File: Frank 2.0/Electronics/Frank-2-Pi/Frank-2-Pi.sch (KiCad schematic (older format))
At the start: 62 parts, among them J1 left wheel sensor, J10 USB-to-controller, J11 power-connector, J12 servo 3, J13 servo 2, J14 servo 1, J15 GPIO, J16 data-connector, J2 Left motor, J3 Right motor, J4 right wheel sensor, J5 Analogue inputs, J6 LIDAR, J7 Phototransistor, J8 USB-from-battery, J9 power switch, Q1 DMN6075S, Q2 DMN6075S, U1 adafruit-2448, U2 LM2903, U3 adafruit-1015, U4 AP1117-33, U5 sparkfun-sx1509

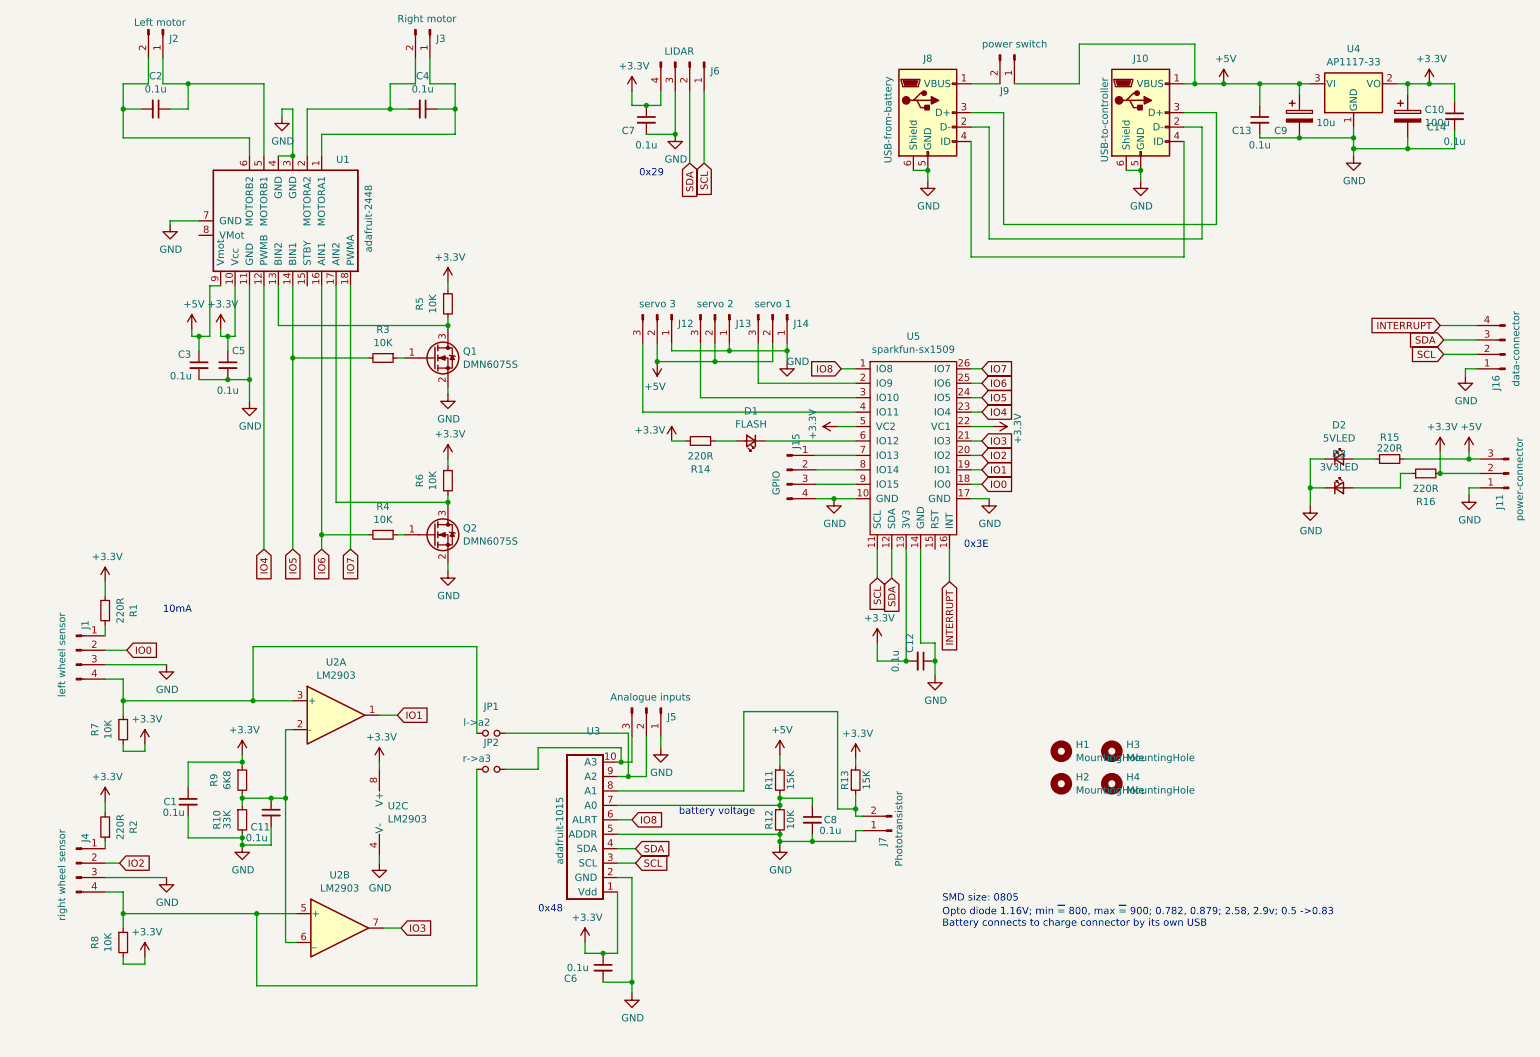
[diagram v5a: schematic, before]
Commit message: PCB finished (but probably not final...) Except for silks
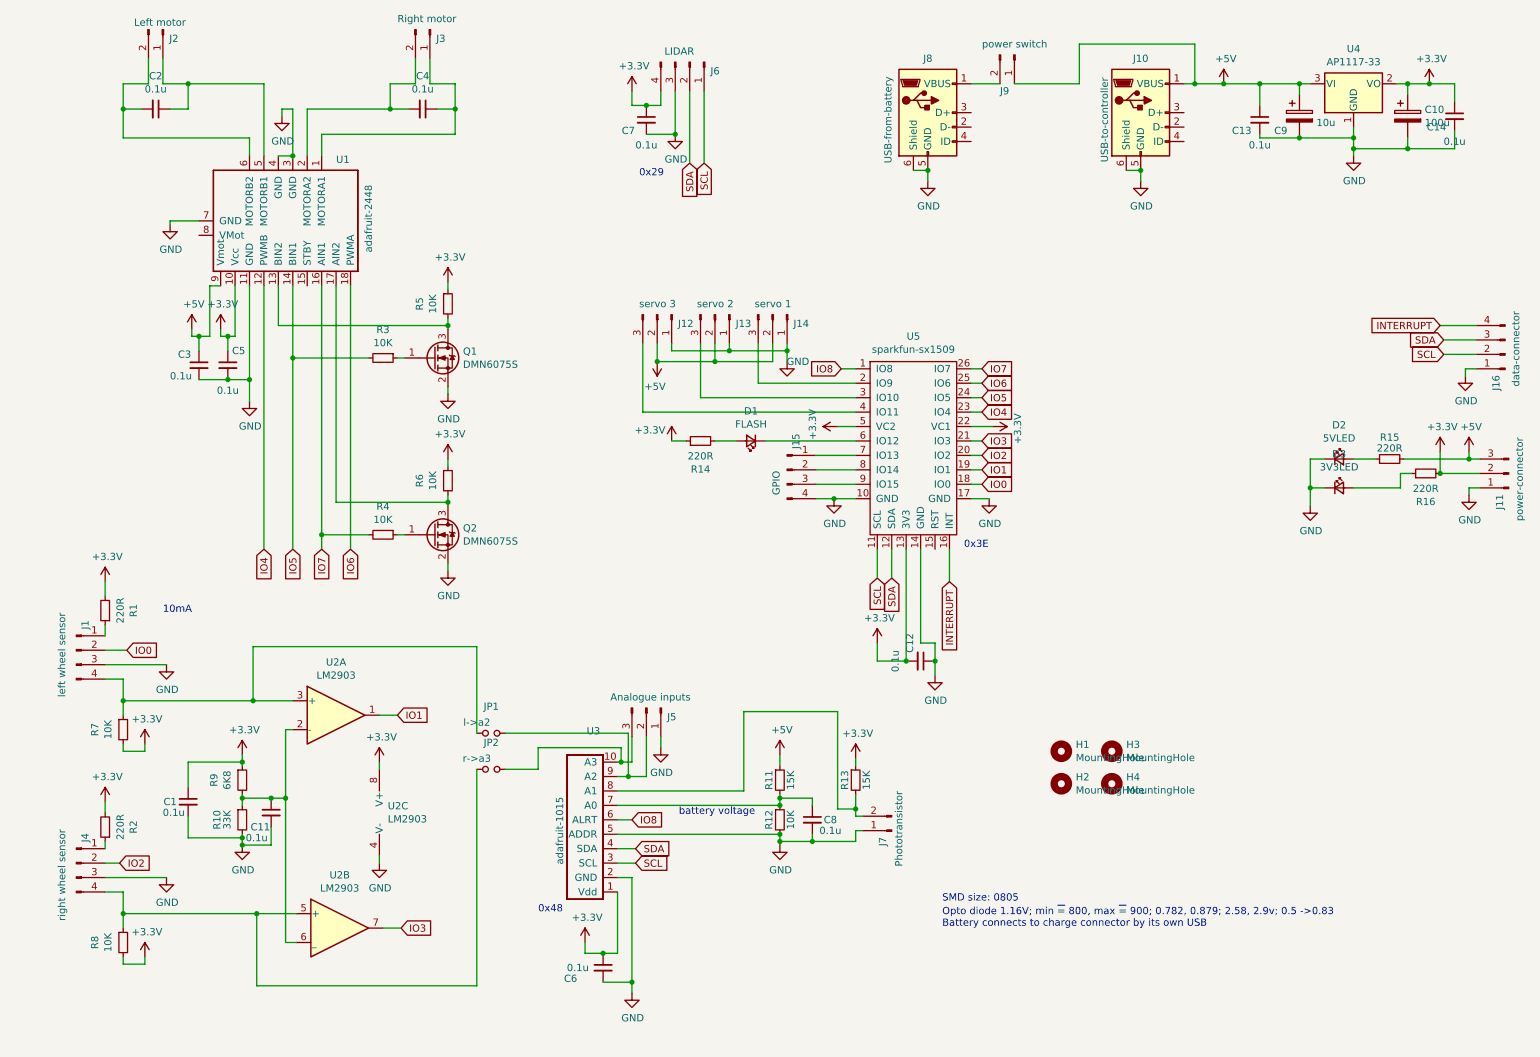
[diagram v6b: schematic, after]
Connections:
- net IO6: now also U1.18 (PWMA); no longer R4.2, U1.16 (AIN1)
- net IO7: now also R4.2, U1.16 (AIN1); no longer U1.18 (PWMA)
- net at J10.2 (D-): no longer J8.2 (D-)
- net at J10.3 (D+): no longer J8.3 (D+)
- net at J10.4 (ID): no longer J8.4 (ID)
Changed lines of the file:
@@
 IO4
 Text GLabel 2925 4225 3    50   Input ~ 0
-IO7
+IO6
 Text GLabel 2525 4225 3    50   Input ~ 0
 IO5
 Text GLabel 2725 4225 3    50   Input ~ 0
-IO6
+IO7
 $Comp
 L Transistor_FET:DMN6075S Q1
@@
 Wire Wire Line
 	8400 1600 8400 1675
-Wire Wire Line
-	8700 1200 8925 1200
-Wire Wire Line
-	8700 1300 8825 1300
 $Comp
 L Connector:USB_OTG J8
@@
 Wire Wire Line
 	6925 1600 6925 1675
-Wire Wire Line
-	7225 1200 7450 1200
-Wire Wire Line
-	7225 1300 7350 1300
-Wire Wire Line
-	8925 1200 8925 1975
-Wire Wire Line
-	7450 1200 7450 1975
-Wire Wire Line
-	8825 1300 8825 2075
-Wire Wire Line
-	7350 1300 7350 2075
-Wire Wire Line
-	7450 1975 8925 1975
-Wire Wire Line
-	7350 2075 8825 2075
 $Comp
 L Connector:Conn_01x02_Male J9
@@
 Wire Wire Line
 	10650 2975 10650 3025
-Wire Wire Line
-	7225 1400 7225 2200
-Wire Wire Line
-	7225 2200 8700 2200
-Wire Wire Line
-	8700 2200 8700 1400
 Text Notes 4925 1650 0    50   ~ 0
 0x29

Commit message: Motor and castor design improvements. I2C pullup resistors added.
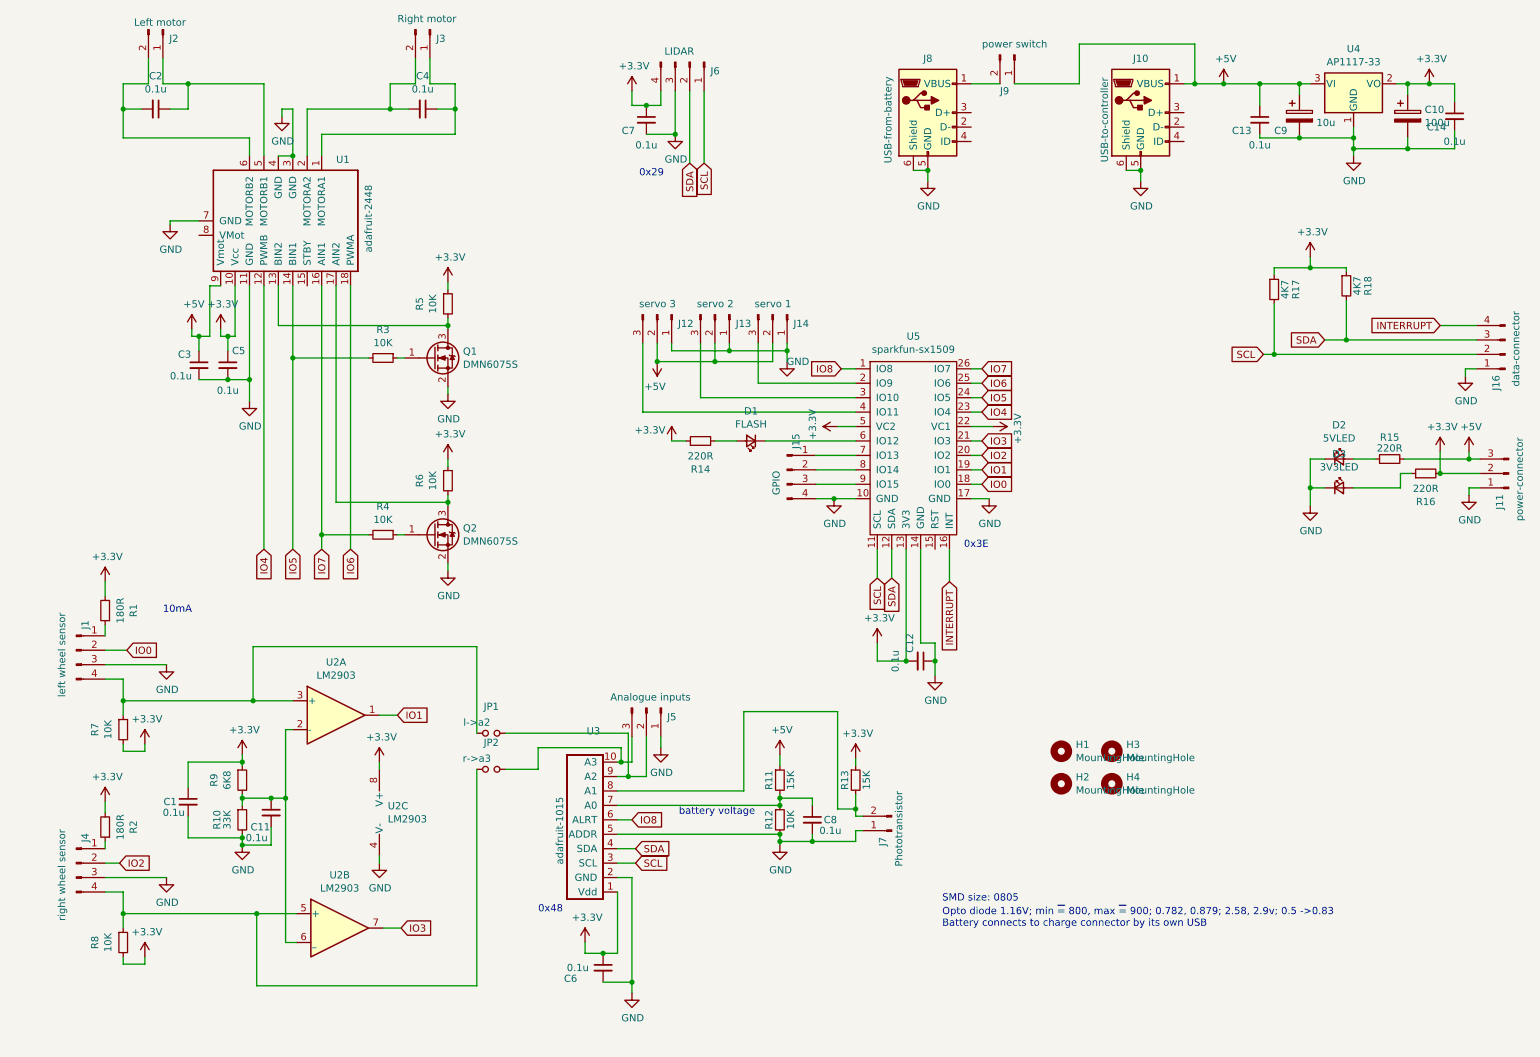
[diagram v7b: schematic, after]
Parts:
- added R17, R18: 4K7, Resistor_SMD:R_0805_2012Metric, symbol Device:R_Small
- R1, R2: value 220R -> 180R
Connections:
- net +3V3: now also R17.1, R18.1
- net SCL: now also R17.2
- net SDA: now also R18.2
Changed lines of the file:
@@
 P 1225 4650
 F 0 "R1" V 1029 4650 50  0000 C CNN
-F 1 "220R" V 1120 4650 50  0000 C CNN
+F 1 "180R" V 1120 4650 50  0000 C CNN
 F 2 "Resistor_SMD:R_0805_2012Metric" H 1225 4650 50  0001 C CNN
 F 3 "~" H 1225 4650 50  0001 C CNN
@@
 P 1225 6150
 F 0 "R2" V 1029 6150 50  0000 C CNN
-F 1 "220R" V 1120 6150 50  0000 C CNN
+F 1 "180R" V 1120 6150 50  0000 C CNN
 F 2 "Resistor_SMD:R_0805_2012Metric" H 1225 6150 50  0001 C CNN
 F 3 "~" H 1225 6150 50  0001 C CNN
@@
 	1    0    0    -1
 $EndComp
-Text GLabel 10500 2775 0    50   Input ~ 0
+Text GLabel 9675 2775 0    50   Input ~ 0
 SDA
-Text GLabel 10500 2875 0    50   Input ~ 0
+Text GLabel 9250 2875 0    50   Input ~ 0
 SCL
-Wire Wire Line
-	10500 2775 10725 2775
-Wire Wire Line
-	10500 2875 10725 2875
 Wire Wire Line
 	10725 2975 10650 2975
@@
 	1    0    0    -1
 $EndComp
+Wire Wire Line
+	9675 2775 9825 2775
+Wire Wire Line
+	10725 2875 9325 2875
+$Comp
+L Device:R_Small R18
+U 1 1 5F395C16
+P 9825 2400
+F 0 "R18" V 9975 2400 50  0000 C CNN
+F 1 "4K7" V 9900 2400 50  0000 C CNN
+F 2 "Resistor_SMD:R_0805_2012Metric" H 9825 2400 50  0001 C CNN
+F 3 "~" H 9825 2400 50  0001 C CNN
+	1    9825 2400
+	1    0    0    -1
+$EndComp
+$Comp
+L Device:R_Small R17
+U 1 1 5F39678A
+P 9325 2425
+F 0 "R17" V 9475 2425 50  0000 C CNN
+F 1 "4K7" V 9400 2425 50  0000 C CNN
+F 2 "Resistor_SMD:R_0805_2012Metric" H 9325 2425 50  0001 C CNN
+F 3 "~" H 9325 2425 50  0001 C CNN
+	1    9325 2425
+	1    0    0    -1
+$EndComp
+Wire Wire Line
+	9825 2500 9825 2775
+Connection ~ 9825 2775
+Wire Wire Line
+	9825 2775 10725 2775
+Wire Wire Line
+	9325 2525 9325 2875
+Connection ~ 9325 2875
+Wire Wire Line
+	9325 2875 9250 2875
+Wire Wire Line
+	9325 2325 9325 2275
+Wire Wire Line
+	9325 2275 9575 2275
+Wire Wire Line
+	9825 2275 9825 2300
+$Comp
+L power:+3.3V #PWR0147
+U 1 1 5F3CD87D
+P 9575 2200
+F 0 "#PWR0147" H 9575 2050 50  0001 C CNN
+F 1 "+3.3V" H 9590 2373 50  0000 C CNN
+F 2 "" H 9575 2200 50  0001 C CNN
+F 3 "" H 9575 2200 50  0001 C CNN
+	1    9575 2200
+	1    0    0    -1
+$EndComp
+Wire Wire Line
+	9575 2200 9575 2275
+Connection ~ 9575 2275
+Wire Wire Line
+	9575 2275 9825 2275
 $EndSCHEMATC

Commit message: PCB as prototyped.
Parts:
- U1: symbol reprapltd-kicad:adafruit-2448 -> Frank-2-Pi-rescue:adafruit-2448-reprapltd-kicad
- U3: symbol reprapltd-kicad:adafruit-1015 -> Frank-2-Pi-rescue:adafruit-1015-reprapltd-kicad
- U5: symbol reprapltd-kicad:sparkfun-sx1509 -> Frank-2-Pi-rescue:sparkfun-sx1509-reprapltd-kicad
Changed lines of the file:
@@
 Opto diode 1.16V; min ~= 800, max ~= 900; 0.782, 0.879; 2.58, 2.9v; 0.5 ->0.83\nBattery connects to charge connector by its own USB
 $Comp
-L reprapltd-kicad:adafruit-2448 U1
+L Frank-2-Pi-rescue:adafruit-2448-reprapltd-kicad U1
 U 1 1 5EC6970C
 P 2475 2000
@@
 10mA
 $Comp
-L reprapltd-kicad:adafruit-1015 U3
+L Frank-2-Pi-rescue:adafruit-1015-reprapltd-kicad U3
 U 1 1 5ECFE0B0
 P 4575 6150
@@
 	10725 2675 10475 2675
 $Comp
-L reprapltd-kicad:sparkfun-sx1509 U5
+L Frank-2-Pi-rescue:sparkfun-sx1509-reprapltd-kicad U5
 U 1 1 5ECC19BD
 P 6825 3525
